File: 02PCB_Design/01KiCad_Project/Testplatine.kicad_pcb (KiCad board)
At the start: 4 copper layers, 231.7 x 129.8 mm, 146 parts, among them J1 RJ45-8N-B, J2 Screw_Terminal_01x03, J3 FCR7350R, J4 FCR7350R, J5 DE9_Receptacle_MountingHoles, J6 Conn_01x06_Pin, J7 RJ45-8N-B, U1 AS5047P-ATSM, U10 INA240A1PW, U11 NUCLEO-G431RB, U12 MCP2562FD, U2 ISM330BXTR, U3 L6982, U4 AP2114D, U5 LMG2100R044RARR, U6 INA240A1PW, U7 LMG2100R044RARR, U8 INA240A1PW, U9 LMG2100R044RARR

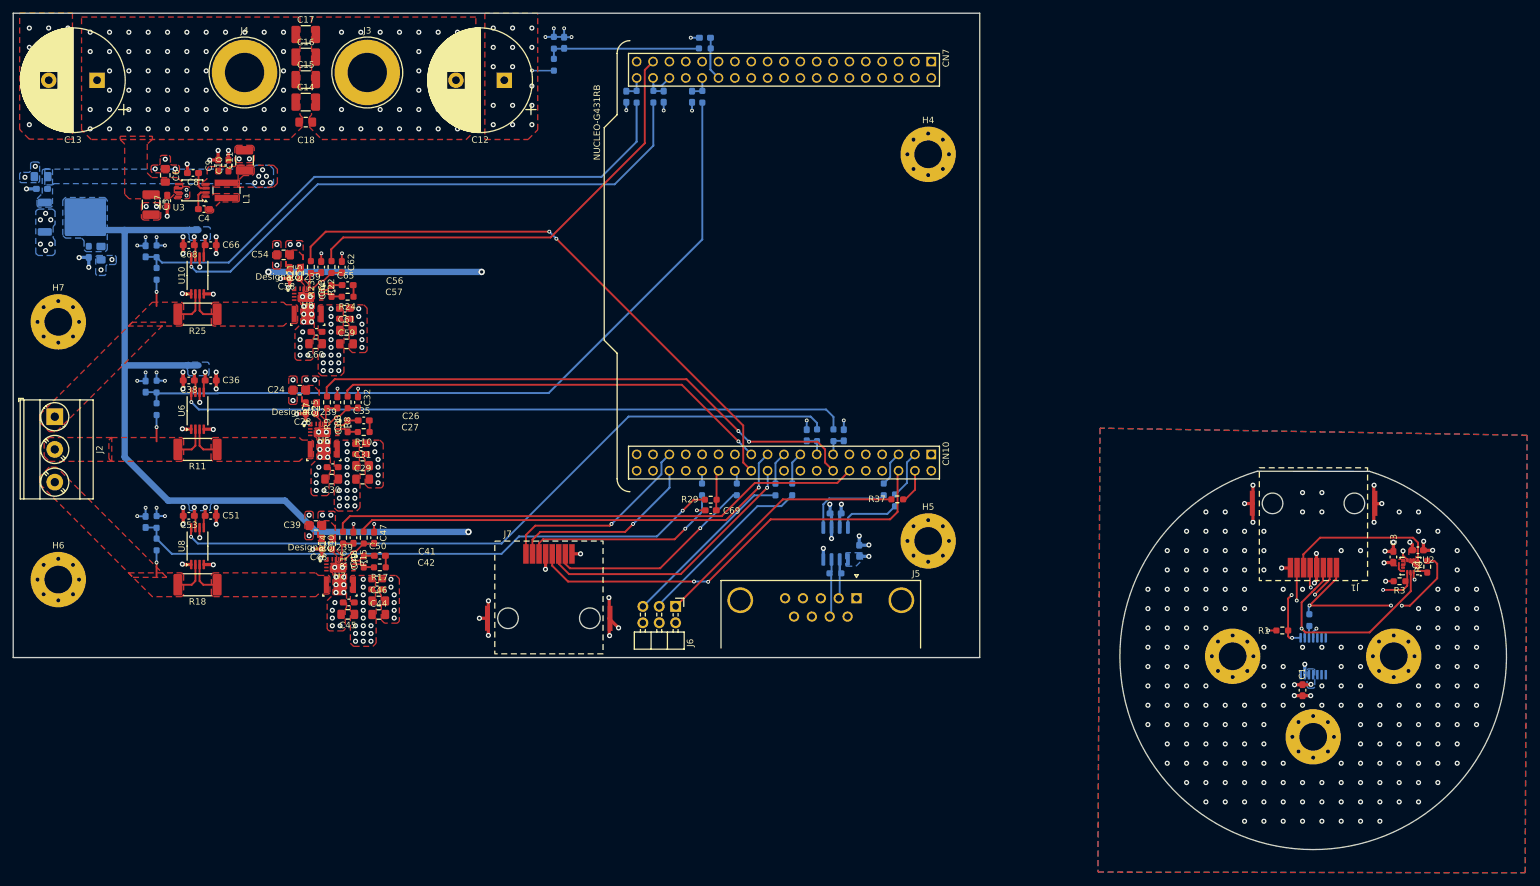
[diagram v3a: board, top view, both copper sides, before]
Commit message: Edited some more footprints and vias
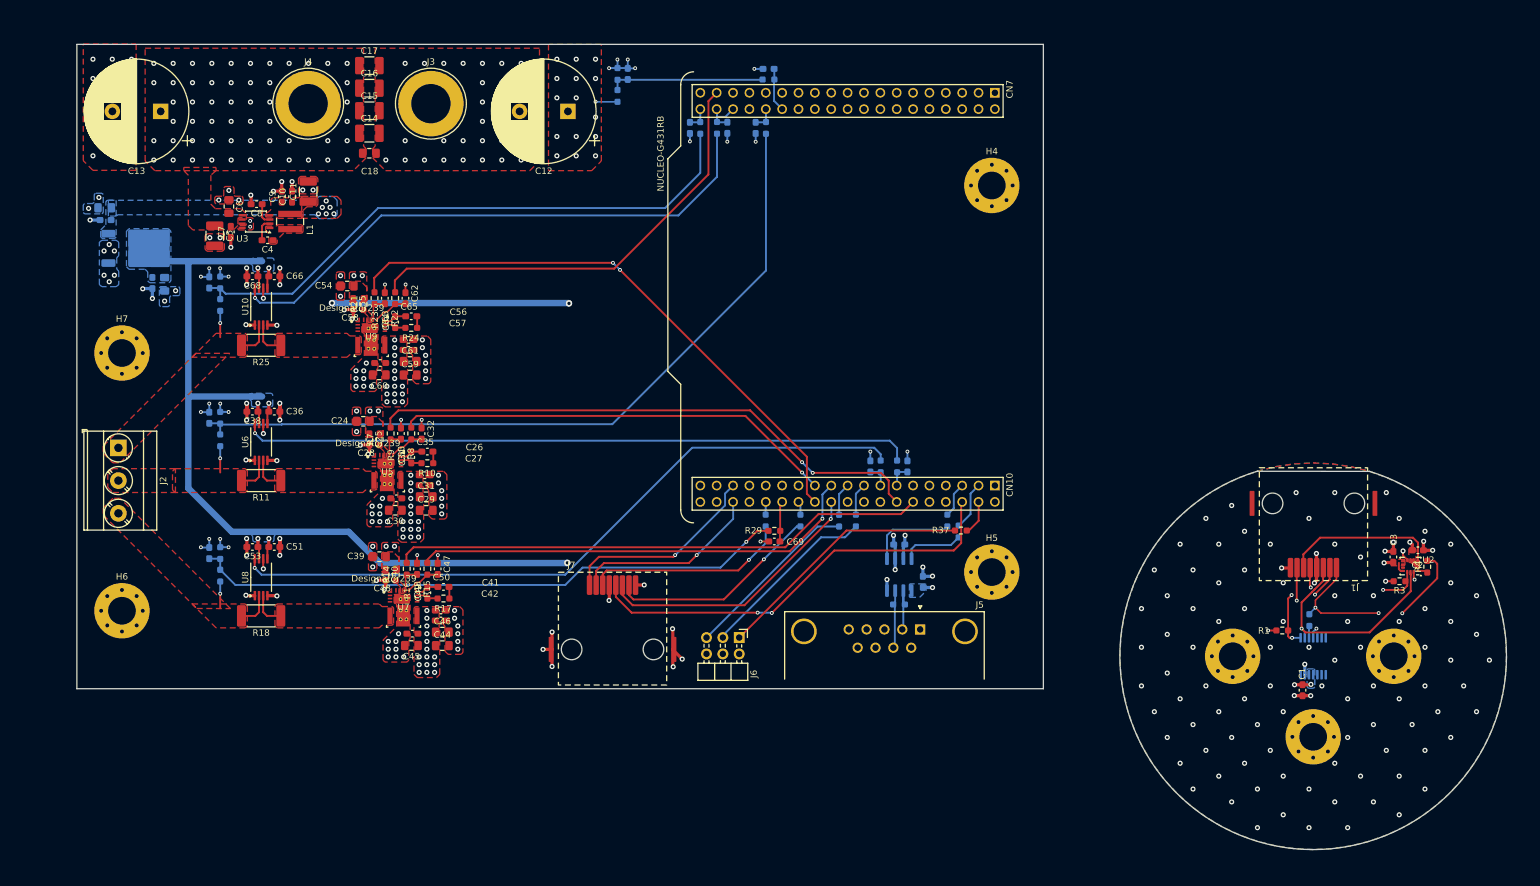
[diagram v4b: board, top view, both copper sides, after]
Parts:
- moved C41 11.0 mm to (106.4, 132.8)
- moved C46 11.0 mm to (106.6, 136.1)
- moved R17 11.0 mm to (106.8, 130.9)
- moved C10 11.0 mm to (83.3, 68.6)
- moved C11 11.0 mm to (85.8, 67.8)
- moved C19 11.0 mm to (54.2, 70.3)
- moved C22 11.0 mm to (63.5, 82.2)
- moved C24 11.0 mm to (94.3, 103.4)
- moved C26 11.0 mm to (103.9, 111.8)
- moved C28 11.0 mm to (99.5, 115.4)
- moved C29 11.0 mm to (104.1, 117.2)
- moved C32 11.0 mm to (103.4, 105.3)
- moved C33 11.0 mm to (100.2, 105.3)
- moved C35 11.0 mm to (104.3, 108.1)
- moved C36 11.0 mm to (80.5, 101.9)
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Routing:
- net GND1: track 30.1 -> 16.0 mm, vias 203 -> 103
- net +3.3V: track 251.2 -> 252.0 mm
- net GNDA: vias 203 -> 189
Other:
- board size 231.7 x 129.8 mm -> 221.9 x 125 mm

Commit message: Edited some connectors
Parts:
- removed H4: MountingHole, MountingHole:MountingHole_4.3mm_M4_Pad_Via
- added C78: 10uF, Capacitor_SMD:C_1206_3216Metric_Pad1.33x1.80mm_HandSolder, F.Cu at (197.2, 99.0)
- added C79: 100nF, Capacitor_SMD:C_0603_1608Metric_Pad1.08x0.95mm_HandSolder, F.Cu at (197.9, 101.0)
- added D1: LED, LED_SMD:LED_0805_2012Metric_Pad1.15x1.40mm_HandSolder, F.Cu at (32.3, 50.8)
- added D2: LED, LED_SMD:LED_0805_2012Metric_Pad1.15x1.40mm_HandSolder, F.Cu at (28.6, 50.8)
- added D3: LED, LED_SMD:LED_0805_2012Metric_Pad1.15x1.40mm_HandSolder, F.Cu at (24.8, 50.8)
- added D4: LED, LED_SMD:LED_0805_2012Metric_Pad1.15x1.40mm_HandSolder, F.Cu at (196.4, 105.0)
- added R43: 47k, Resistor_SMD:R_1206_3216Metric_Pad1.30x1.75mm_HandSolder, F.Cu at (32.5, 46.2)
- added R44: 3.3k, Resistor_SMD:R_0805_2012Metric_Pad1.20x1.40mm_HandSolder, F.Cu at (28.6, 46.8)
- added R45: 2.2k, Resistor_SMD:R_0805_2012Metric_Pad1.20x1.40mm_HandSolder, F.Cu at (24.8, 46.8)
- added R46: 2.2k, Resistor_SMD:R_0805_2012Metric_Pad1.20x1.40mm_HandSolder, F.Cu at (198.7, 105.0)
- J1, J7: value RJ45-8N-B -> Wurth-634008
- J3, J4: value FCR7350R -> RS Pro 304-02-818; footprint Connector:Banana_Jack_1Pin -> MyFootprintLib:FCR7350
- moved C35 42.0 mm to (71.3, 82.1)
- moved C49 42.0 mm to (71.3, 104.0)
- moved C50 42.0 mm to (73.8, 103.1)
- moved C65 42.0 mm to (68.8, 61.1)
- moved C70 42.0 mm to (112.1, 31.9)
- moved H1 42.0 mm to (221.3, 113.9)
- moved H2 42.0 mm to (208.8, 126.4)
- moved H3 42.0 mm to (196.3, 113.9)
- moved R1 42.0 mm to (204.0, 109.9)
- moved R15 42.0 mm to (71.3, 100.3)
- moved R17 42.0 mm to (73.8, 104.9)
- moved R22 42.0 mm to (66.3, 58.3)
- moved R24 42.0 mm to (68.8, 62.9)
- moved R28 42.0 mm to (123.8, 92.8)
- moved R30 42.0 mm to (129.2, 92.8)
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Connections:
- H5 pad 1: (no net) -> GNDA
- H6 pad 1: (no net) -> GNDA
- H7 pad 1: (no net) -> GNDA
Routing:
- net +3.3V: track 252.0 -> 294.7 mm, vias 9 -> 11
- net +5V: track 218.5 -> 227.4 mm
- net +24V: track 3.42 -> 8.03 mm
- net GND1: track 16.0 -> 19.1 mm, vias 103 -> 100
- net +3.3VP: track 77.8 -> 80.2 mm, vias 7 -> 12
- net Net-(D4-A): track 0.00 -> 2.27 mm
- net Net-(D3-A): track 0.00 -> 2.00 mm
- net Net-(D2-A): track 0.00 -> 1.97 mm
- net Net-(D1-A): track 0.00 -> 1.85 mm
- net /escSheet/HalfBridgePowerStage3/PWM_LI: track 90.4 -> 89.6 mm
- net GNDA: track 123.9 -> 123.6 mm, vias 189 -> 192
- added copper zone on In2.Cu, net +3.3VP
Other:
- outline, holes or cut-outs redrawn

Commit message: relayout in progress
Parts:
- removed D1, D2: LED, LED_SMD:LED_0805_2012Metric_Pad1.15x1.40mm_HandSolder
- removed R43: 47k, Resistor_SMD:R_1206_3216Metric_Pad1.30x1.75mm_HandSolder
- removed R44: 3.3k, Resistor_SMD:R_0805_2012Metric_Pad1.20x1.40mm_HandSolder
- added R47: 0R, Resistor_SMD:R_0603_1608Metric_Pad0.98x0.95mm_HandSolder, B.Cu at (179.0, 119.2)
- added R48: 0R, Resistor_SMD:R_0603_1608Metric_Pad0.98x0.95mm_HandSolder, B.Cu at (180.8, 119.2)
- C10, C8: footprint Capacitor_SMD:C_0603_1608Metric_Pad1.08x0.95mm_HandSolder -> Capacitor_SMD:C_0805_2012Metric_Pad1.18x1.45mm_HandSolder
- C25, C34, C35, C36, C38, C40, C49, C50, C51, C53, C55, C64, C65, C66, C68, C76, C77: value 0.1uF -> 100nF
- C32, C33, C47, C48, C62, C63: value 47p -> 47pF
- C78: footprint Capacitor_SMD:C_1206_3216Metric_Pad1.33x1.80mm_HandSolder -> Capacitor_SMD:C_1210_3225Metric_Pad1.33x2.70mm_HandSolder
- J2: value Screw_Terminal_01x03 -> Wurth Elektronic 2365 Printklemme; footprint TerminalBlock_Phoenix:TerminalBlock_Phoenix_MKDS-3-3-5.08_1x03_P5.08mm_Horizontal -> MyFootprintLib:Wurth Elektronik 2365 Printklemme
- J5: value DE9_Receptacle_MountingHoles -> RS PRO 528 D-Sub 2.77mm
- R11, R18, R25: value 3.3m -> 3m
- R15, R16, R22, R23, R8, R9: value 20 -> 20R
- R42: value 120 -> 120R
- U12: value MCP2562FD -> MCP2562FD-E/MF; footprint Package_SO:SOIC-8_3.9x4.9mm_P1.27mm -> Package_DFN_QFN:DFN-8-1EP_3x3mm_P0.65mm_EP1.55x2.4mm
- U3: value L6982 -> L6982C50DR
- moved C24 46.0 mm to (105.6, 90.0), turned to 90 degrees
- moved C25 44.0 mm to (104.3, 93.7)
- moved C26 44.0 mm to (112.8, 99.3)
- moved C27 44.0 mm to (112.8, 100.8)
- moved C28 44.0 mm to (108.4, 102.9)
- moved C29 44.0 mm to (113.1, 104.7)
- moved C30 44.0 mm to (108.3, 104.7)
- moved C31 44.0 mm to (113.1, 102.6)
- moved C32 44.0 mm to (112.4, 92.8)
- moved C33 44.0 mm to (109.2, 92.8)
- moved C34 44.0 mm to (110.8, 96.5)
- moved C35 44.0 mm to (113.3, 95.6)
- moved R10 44.0 mm to (113.3, 97.4)
- moved R7 44.0 mm to (105.9, 93.7)
- moved R8 44.0 mm to (110.8, 92.8)
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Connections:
- J5 pad 2: Net-(U12-CANL) -> Net-(J5-Pad2)
- J5 pad 7: Net-(U12-CANH) -> Net-(J5-Pad7)
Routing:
- net GNDA: track 123.6 -> 105.0 mm, vias 192 -> 186
- net /escSheet/HalfBridgePowerStage1/PWM_HI: track 68.5 -> 61.6 mm
- net /escSheet/HalfBridgePowerStage1/PWM_LI: track 88.0 -> 81.2 mm
- net Net-(J5-Pad7): track 0.00 -> 5.97 mm
- net /escSheet/HalfBridgePowerStage2/PWM_LI: track 82.9 -> 88.7 mm
- net /escSheet/HalfBridgePowerStage2/PWM_HI: track 69.7 -> 75.2 mm
- net Net-(U12-CANH): track 8.69 -> 3.35 mm
- net Net-(U12-CANL): track 7.77 -> 3.33 mm
- net +3.3V: track 294.7 -> 298.9 mm
- net +24V: track 8.03 -> 3.93 mm
- net Net-(J5-Pad2): track 0.00 -> 3.31 mm
- net GND1: track 19.1 -> 16.0 mm, vias 100 -> 101
- net +5V: track 227.4 -> 229.7 mm, vias 15 -> 11
- net Net-(D3-A): track 2.00 -> 0.00 mm
- net Net-(D2-A): track 1.97 -> 0.00 mm
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- removed copper zone on In2.Cu, net +5V
- removed copper zone on F.Cu, net /escSheet/HalfBridgePowerStage2/SW
- removed copper zone on F.Cu, net /escSheet/HalfBridgePowerStage3/SW
- removed copper zone on F.Cu, net Net-(U7-VCC)
- removed copper zone on F.Cu, net Net-(U9-VCC)

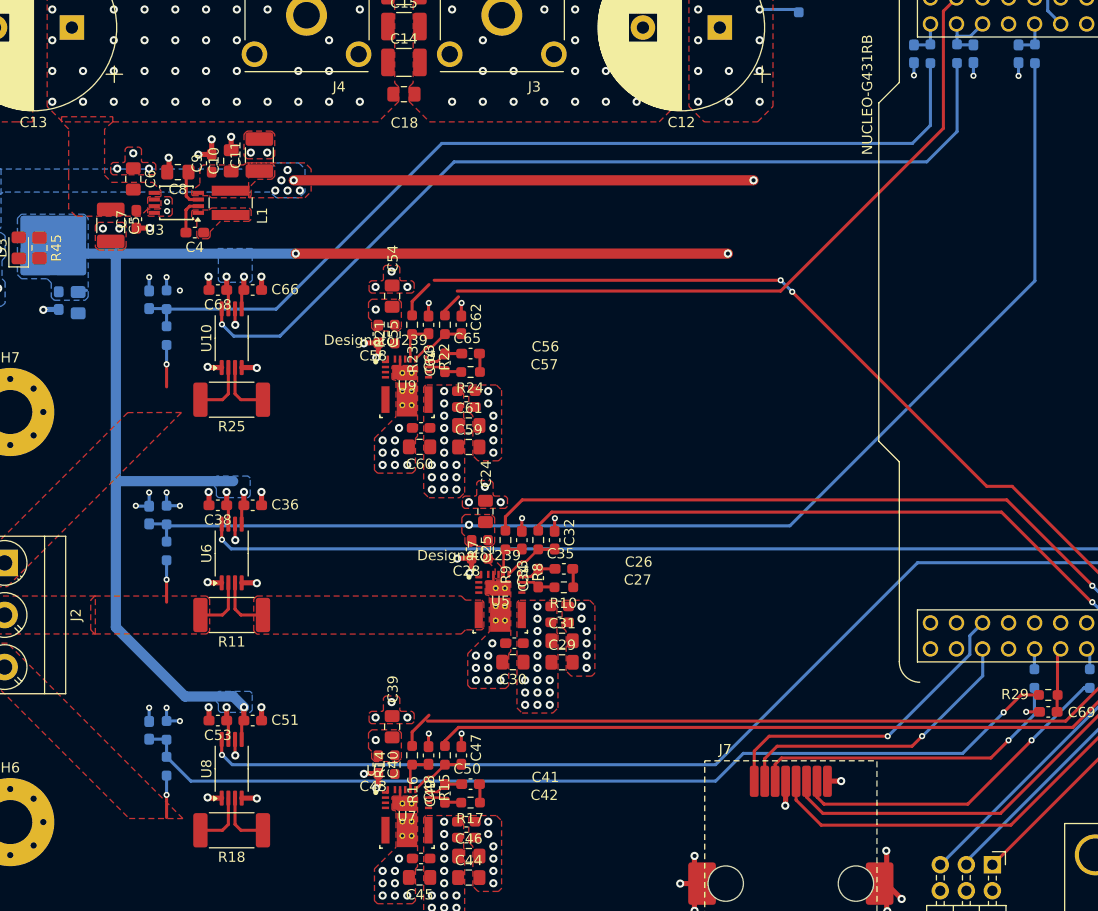
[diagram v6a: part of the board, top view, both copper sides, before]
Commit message: Edited Power Network
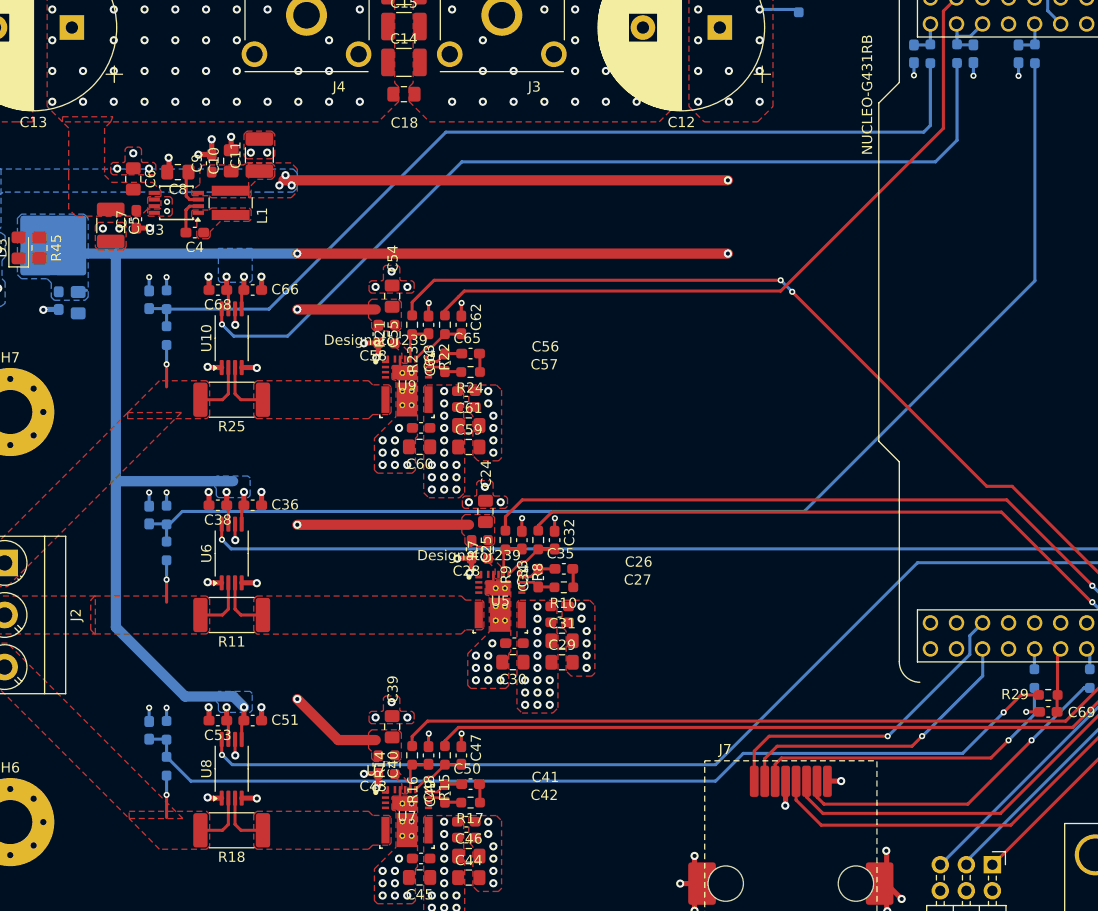
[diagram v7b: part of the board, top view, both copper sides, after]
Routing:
- net +5V: track 229.7 -> 319.4 mm, vias 11 -> 8
- net GNDA: track 105.0 -> 101.1 mm, vias 186 -> 183
- net +3.3V: track 298.9 -> 301.5 mm, vias 11 -> 10
- net /escSheet/HalfBridgePowerStage3/PWM_LI: track 88.3 -> 88.9 mm
- net /escSheet/HalfBridgePowerStage2/PWM_LI: track 88.7 -> 88.1 mm
- added copper zone on In2.Cu, net +5V
- added copper zone on F.Cu, net /escSheet/HalfBridgePowerStage2/SW
- added copper zone on F.Cu, net /escSheet/HalfBridgePowerStage3/SW
- added copper zone on F.Cu, net Net-(U7-VCC)
- added copper zone on F.Cu, net Net-(U9-VCC)

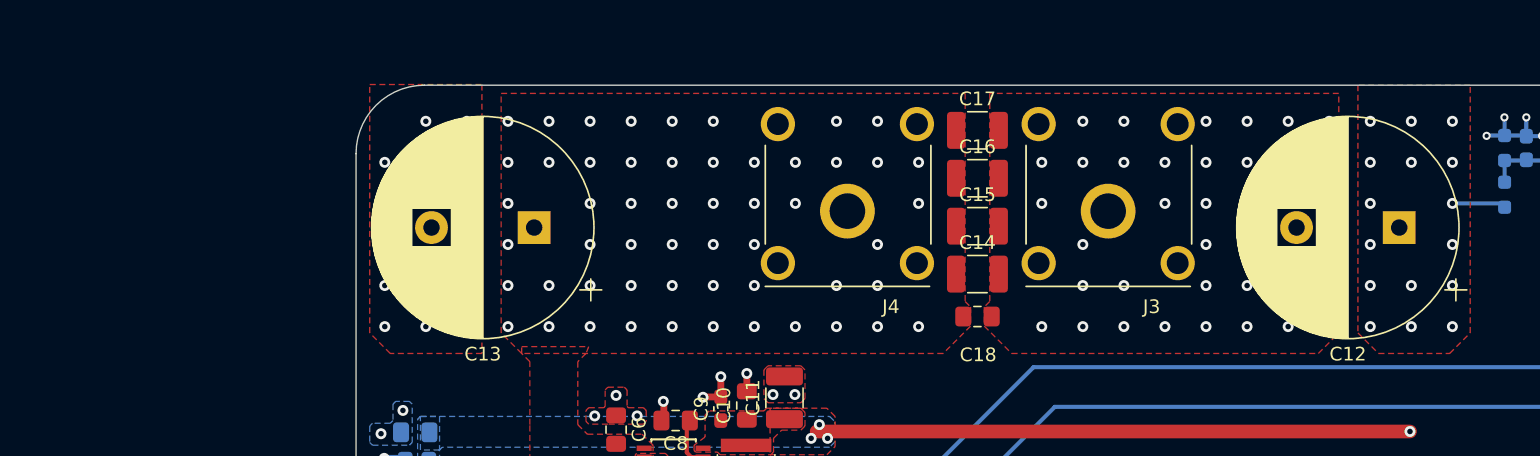
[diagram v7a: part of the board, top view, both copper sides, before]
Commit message: added ideal diode in schematic
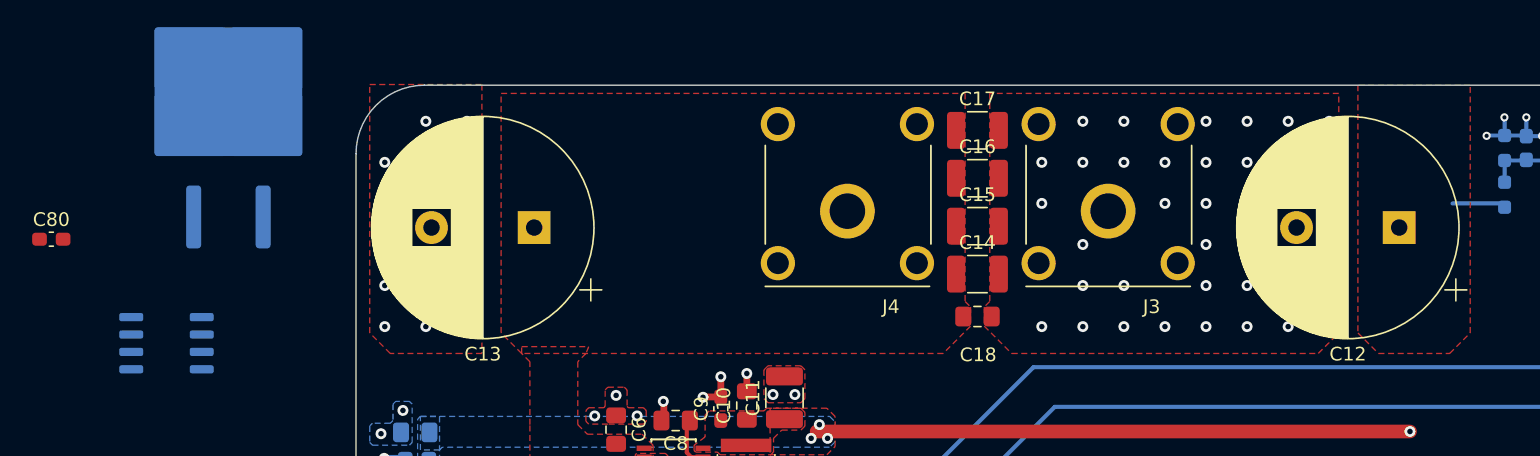
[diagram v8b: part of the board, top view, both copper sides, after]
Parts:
- added C80: 47nF, Capacitor_SMD:C_0603_1608Metric_Pad1.08x0.95mm_HandSolder, F.Cu at (30.0, 43.7)
- added Q1: AUIRFS4310ZTRL, Package_TO_SOT_SMD:TO-263-2, B.Cu at (42.9, 34.4)
- added U13: LTC4359, Package_SO:SO-8_3.9x4.9mm_P1.27mm, B.Cu at (38.4, 51.3)
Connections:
- J4 pad 1: +24V -> Net-(U13-IN)
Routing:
- net +24V: vias 115 -> 45
